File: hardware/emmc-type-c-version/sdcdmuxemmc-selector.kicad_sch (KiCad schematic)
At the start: 31 parts, among them U501 93LCxxBxxOT, U502 FT232HL, Y501 12MHz

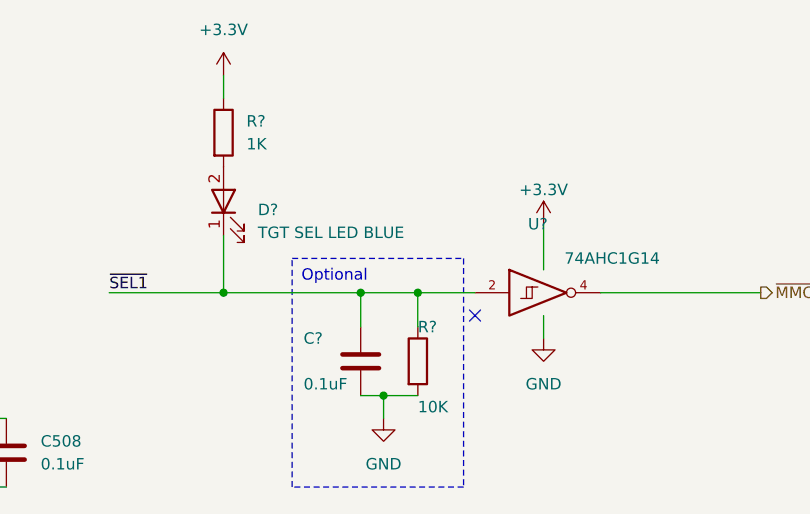
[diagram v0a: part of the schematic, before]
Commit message: Corrected part number in the BOM
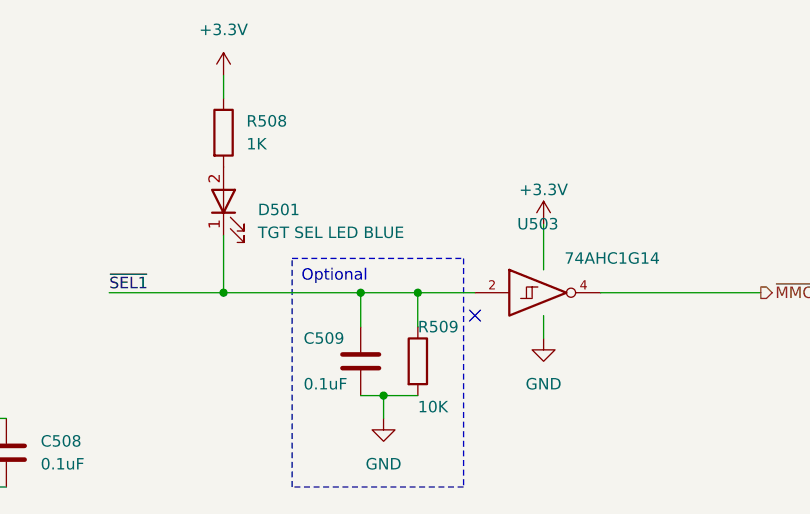
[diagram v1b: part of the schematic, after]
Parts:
- C513, C514, C515: digikey 311-1455-1-ND -> 490-14466-1-ND; storeURL https://www.digikey.com/en/products/detail/yageo/CC0603KRX5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 -> https://www.digikey.com/en/products/detail/murata-electroni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
- FB501, FB502: footprint Inductor_SMD:L_0805_2012Metric_Pad1.15x1.40mm_HandSolder -> Inductor_SMD:L_0603_1608Metric_Pad1.05x0.95mm_HandSolder; digikey 240-2399-1-ND -> 490-1014-1-ND; storeURL https://www.digikey.com/en/products/detail/laird-signal-int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 -> https://www.digikey.com/en/products/detail/murata-electroni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
- R501: footprint tbctl:R_0805_2012Metric_Pad1.20x1.40mm_HandSolder -> Resistor_SMD:R_0805_2012Metric_Pad1.20x1.40mm_HandSolder; digikey 311-12.0KHRCT-ND -> 311-12.0KCRCT-ND; storeURL https://www.digikey.com/en/products/detail/yageo/RC0603FR-0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 -> https://www.digikey.com/en/products/detail/yageo/RC0805FR-0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
- R502, R503, R507: footprint tbctl:R_0805_2012Metric_Pad1.20x1.40mm_HandSolder -> Resistor_SMD:R_0805_2012Metric_Pad1.20x1.40mm_HandSolder; digikey 13-RC0603JR-1010KLCT-ND -> 311-10KARCT-ND; storeURL https://www.digikey.com/en/products/detail/yageo/RC0603JR-1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 -> https://www.digikey.com/en/products/detail/yageo/RC0805JR-0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
- R506: footprint tbctl:R_0805_2012Metric_Pad1.20x1.40mm_HandSolder -> Resistor_SMD:R_0805_2012Metric_Pad1.20x1.40mm_HandSolder; digikey 311-2.0KGRCT-ND -> 311-2.0KARCT-ND; storeURL https://www.digikey.com/en/products/detail/yageo/RC0603JR-0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 -> https://www.digikey.com/en/products/detail/yageo/RC0805JR-0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
- R508: renamed from R?; footprint tbctl:R_0805_2012Metric_Pad1.20x1.40mm_HandSolder -> Resistor_SMD:R_0805_2012Metric_Pad1.20x1.40mm_HandSolder; digikey 13-RC0603JR-101KLCT-ND -> 311-1.0KARCT-ND; storeURL https://www.digikey.com/en/products/detail/yageo/RC0603JR-1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 -> https://www.digikey.com/en/products/detail/yageo/RC0805JR-0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
- R509: renamed from R?; footprint tbctl:R_0805_2012Metric_Pad1.20x1.40mm_HandSolder -> Resistor_SMD:R_0805_2012Metric_Pad1.20x1.40mm_HandSolder; digikey 13-RC0603JR-1010KLCT-ND -> 311-10KARCT-ND; storeURL https://www.digikey.com/en/products/detail/yageo/RC0603JR-1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 -> https://www.digikey.com/en/products/detail/yageo/RC0805JR-0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
- gave numbers to parts that had none: 3
